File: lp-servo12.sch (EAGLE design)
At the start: 63 parts, among them J1 M10", J2 M10", J3 M10", J4 M10", U1 TPS54526PWP, U2 LMV358

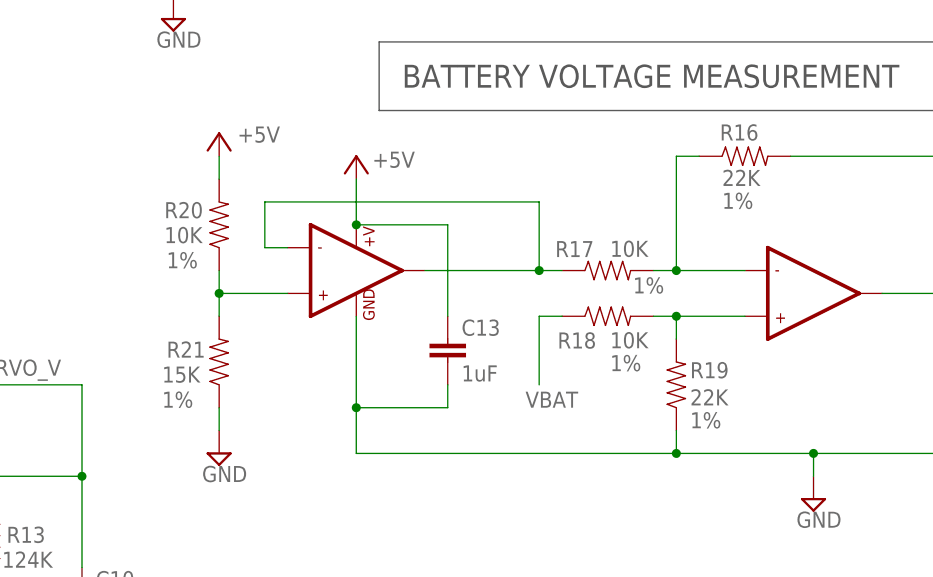
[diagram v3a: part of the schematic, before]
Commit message: Fixed some resistor values on the voltage measuring op-amp circuit. The orginal values were not correct for a 2S battery (they were for a 1S battery). Updated the bom files to reflect the changes in the resistor values. Net effect is that two 22K resistors go away and 2 30K are added, some ref designators change.
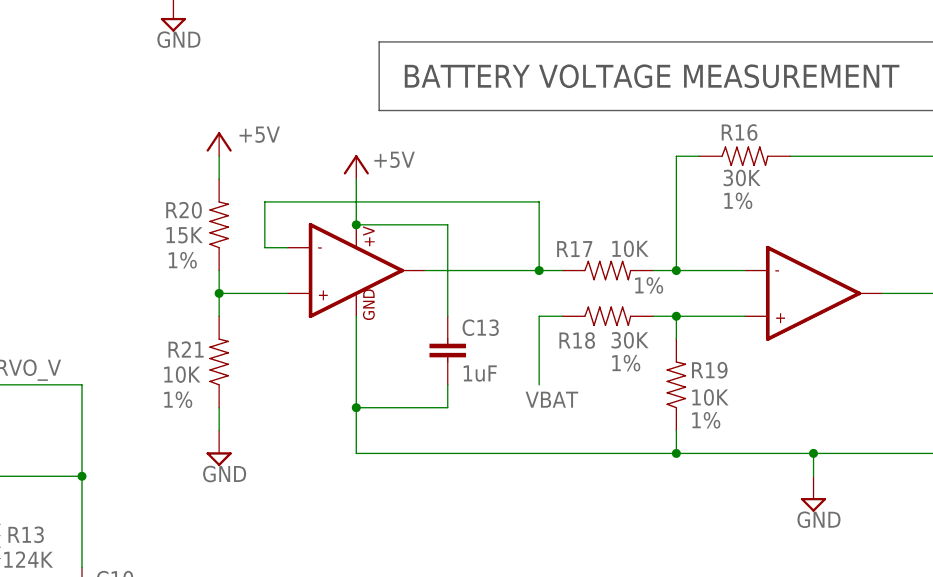
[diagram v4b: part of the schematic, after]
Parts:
- R16: value 22K -> 30K; PARTNO RES_22K_20V_1PCT_0805 -> RES_30K_20V_1PCT_0805
- R18: value 10K -> 30K; PARTNO RES_10K_20V_1PCT_0805 -> RES_30K_20V_1PCT_0805
- R19: value 22K -> 10K; PARTNO RES_22K_20V_1PCT_0805 -> RES_10K_20V_1PCT_0805
- R20: value 10K -> 15K; PARTNO RES_10K_20V_1PCT_0805 -> RES_15K_20V_1PCT_0805
- R21: value 15K -> 10K; PARTNO RES_15K_20V_1PCT_0805 -> RES_10K_20V_1PCT_0805
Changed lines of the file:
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@@
 <attribute name="PARTNO" value="LMV358QDR"/>
 </part>
-<part name="R16" library="SparkFun-Resistors" deviceset="RESISTOR" device="0805-RES" value="22K">
-<attribute name="PARTNO" value="RES_22K_20V_1PCT_0805"/>
+<part name="R16" library="SparkFun-Resistors" deviceset="RESISTOR" device="0805-RES" value="30K">
+<attribute name="PARTNO" value="RES_30K_20V_1PCT_0805"/>
 <attribute name="SIZE" value="(0805)"/>
 <attribute name="TOL" value="1%"/>
@@
 <attribute name="VOLT" value="20V"/>
 </part>
-<part name="R18" library="SparkFun-Resistors" deviceset="RESISTOR" device="0805-RES" value="10K">
+<part name="R18" library="SparkFun-Resistors" deviceset="RESISTOR" device="0805-RES" value="30K">
+<attribute name="PARTNO" value="RES_30K_20V_1PCT_0805"/>
+<attribute name="SIZE" value="(0805)"/>
+<attribute name="TOL" value="1%"/>
+<attribute name="VOLT" value="20V"/>
+</part>
+<part name="R19" library="SparkFun-Resistors" deviceset="RESISTOR" device="0805-RES" value="10K">
 <attribute name="PARTNO" value="RES_10K_20V_1PCT_0805"/>
 <attribute name="SIZE" value="(0805)"/>
@@
 <attribute name="VOLT" value="20V"/>
 </part>
-<part name="R19" library="SparkFun-Resistors" deviceset="RESISTOR" device="0805-RES" value="22K">
-<attribute name="PARTNO" value="RES_22K_20V_1PCT_0805"/>
+<part name="SUPPLY13" library="supply2" deviceset="GND" device=""/>
+<part name="R20" library="SparkFun-Resistors" deviceset="RESISTOR" device="0805-RES" value="15K">
+<attribute name="PARTNO" value="RES_15K_20V_1PCT_0805"/>
 <attribute name="SIZE" value="(0805)"/>
 <attribute name="TOL" value="1%"/>
 <attribute name="VOLT" value="20V"/>
 </part>
-<part name="SUPPLY13" library="supply2" deviceset="GND" device=""/>
-<part name="R20" library="SparkFun-Resistors" deviceset="RESISTOR" device="0805-RES" value="10K">
+<part name="R21" library="SparkFun-Resistors" deviceset="RESISTOR" device="0805-RES" value="10K">
 <attribute name="PARTNO" value="RES_10K_20V_1PCT_0805"/>
 <attribute name="SIZE" value="(0805)"/>
 <attribute name="TOL" value="1%"/>
-<attribute name="VOLT" value="20V"/>
-</part>
-<part name="R21" library="SparkFun-Resistors" deviceset="RESISTOR" device="0805-RES" value="15K">
-<attribute name="PARTNO" value="RES_15K_20V_1PCT_0805"/>
-<attribute name="SIZE" value="(0805)"/>
-<attribute name="TOL" value="1%"/>

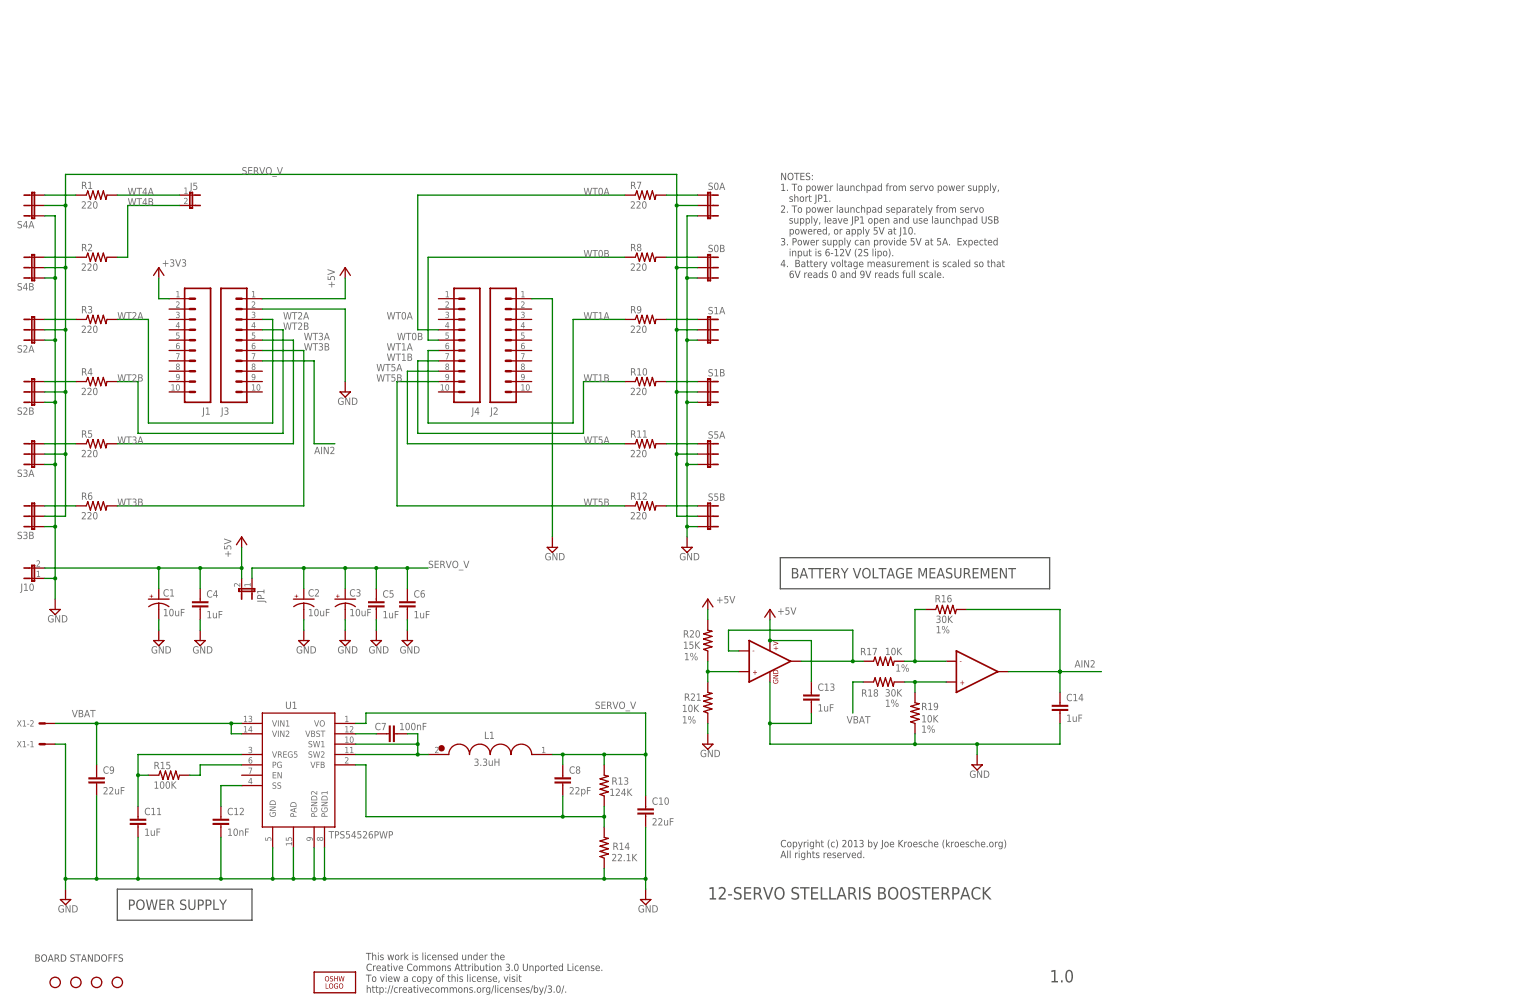
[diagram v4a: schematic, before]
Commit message: Fixed missing pullup on enable line and unconnectd trace on feeback signal for power supply.  Those were the two known bugs. Also moved one of the moounting holes and moved the power connector around so that it would not overhang the edge of the board, and also changed the orientation to come out the top instead of the side.
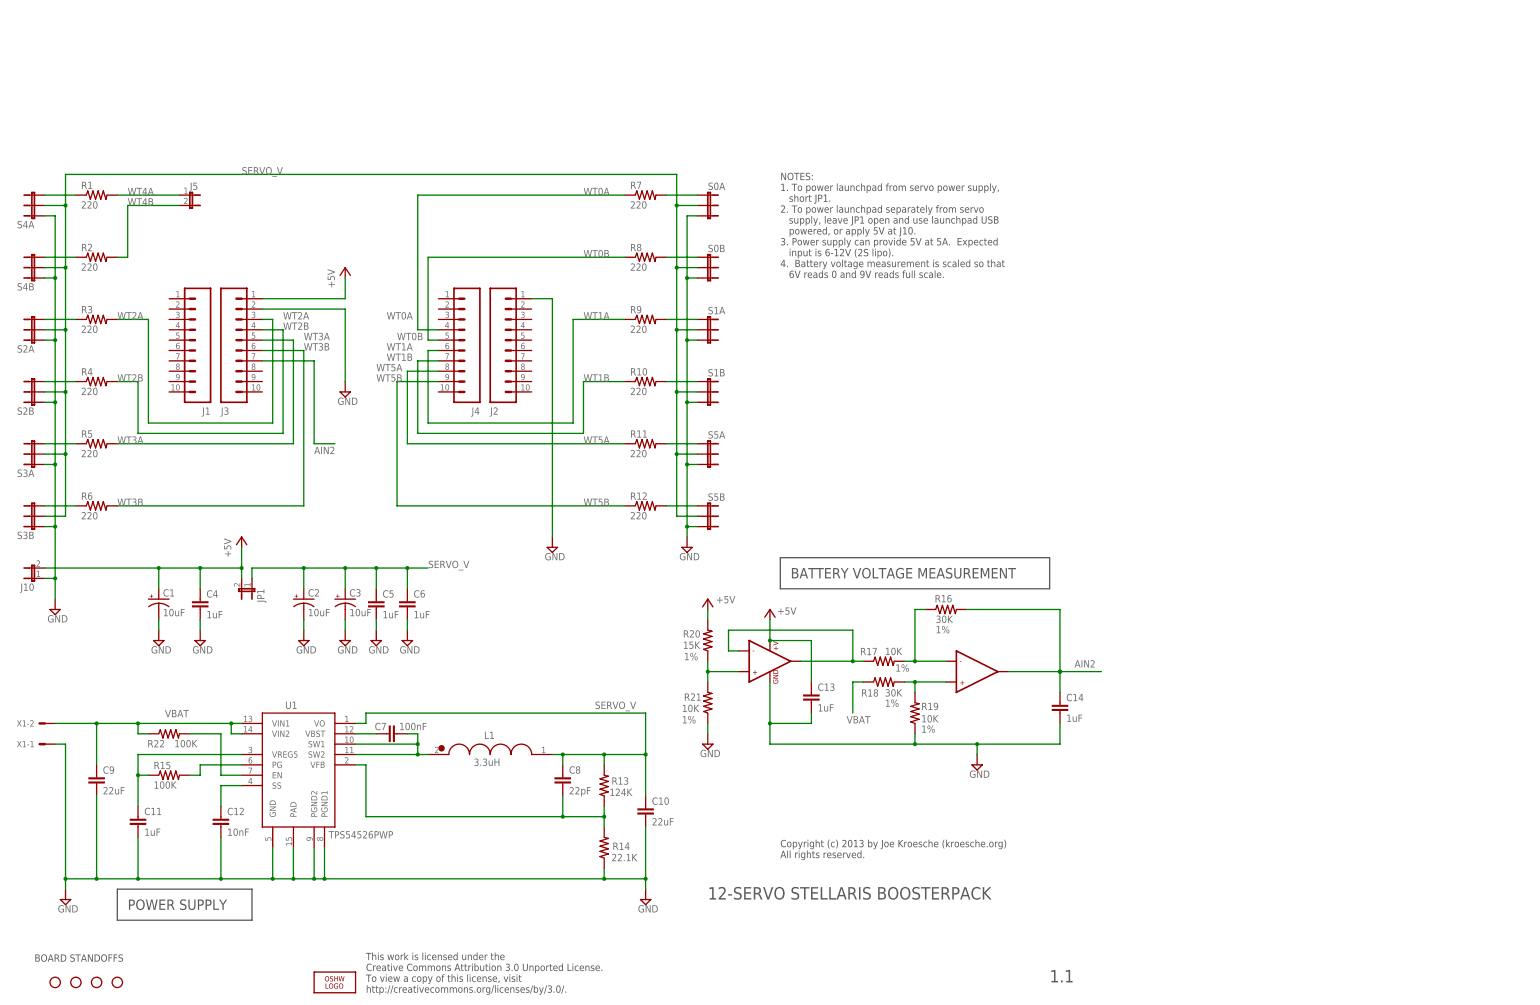
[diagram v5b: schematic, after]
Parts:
- added R22: 100K, SparkFun-Resistors:RESISTOR0805-RES
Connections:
- removed net +3V3: J1.1
- new net N$19: R22.2, U1.EN
- net VBAT: now also R22.1
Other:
- note added: "1.1"
- note removed: "1.0"
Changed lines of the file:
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@@
 <part name="SUPPLY1" library="supply2" deviceset="GND" device=""/>
 <part name="SUPPLY2" library="supply2" deviceset="GND" device=""/>
-<part name="+3V1" library="supply1" deviceset="+3V3" device=""/>
 <part name="P+1" library="supply1" deviceset="+5V" device=""/>
 <part name="SUPPLY3" library="supply2" deviceset="GND" device=""/>
@@
 </part>
 <part name="FRAME2" library="frames" deviceset="FRAME_A_L" device=""/>
+<part name="R22" library="SparkFun-Resistors" deviceset="RESISTOR" device="0805-RES" value="100K">
+<attribute name="PARTNO" value="RES_100K_20V_1PCT_0805"/>
+<attribute name="RATE" value="1/8W"/>
+<attribute name="SIZE" value="(0805)"/>
+<attribute name="TOL" value="1%"/>
+<attribute name="VOLT" value="20V"/>
+</part>
 </parts>
 <sheets>
@@
 4.  Battery voltage measurement is scaled so that
    6V reads 0 and 9V reads full scale.</text>
-<text x="261.62" y="7.62" size="3.048" layer="97" font="vector">1.0</text>
+<text x="261.62" y="7.62" size="3.048" layer="97" font="vector">1.1</text>
 </plain>
 <instances>
 <instance part="SUPPLY1" gate="GND" x="88.9" y="152.4"/>
 <instance part="SUPPLY2" gate="GND" x="139.7" y="114.3"/>
-<instance part="+3V1" gate="G$1" x="43.18" y="182.88" smashed="yes">
-<attribute name="VALUE" x="43.942" y="183.134" size="1.778" layer="96"/>
-</instance>
 <instance part="P+1" gate="1" x="88.9" y="182.88"/>
 <instance part="SUPPLY3" gate="GND" x="17.78" y="99.06"/>
@@
 <instance part="FRAME2" gate="G$1" x="0" y="0"/>
 <instance part="FRAME2" gate="G$2" x="172.72" y="0"/>
+<instance part="R22" gate="G$1" x="45.72" y="68.58" smashed="yes">
+<attribute name="PARTNO" x="45.72" y="68.58" size="1.778" layer="96" display="off"/>
+<attribute name="RATE" x="45.72" y="68.58" size="1.778" layer="96" display="off"/>
+<attribute name="SIZE" x="45.72" y="68.58" size="1.778" layer="96" display="off"/>
+<attribute name="TOL" x="45.72" y="68.58" size="1.778" layer="96" display="off"/>
+<attribute name="VOLT" x="45.72" y="68.58" size="1.778" layer="96" display="off"/>
+<attribute name="NAME" x="40.386" y="65.2526" size="1.778" layer="95"/>
+<attribute name="VALUE" x="46.99" y="65.278" size="1.778" layer="96"/>
+</instance>
 </instances>
 <busses>
@@
 <pinref part="SUPPLY14" gate="GND" pin="GND"/>
 <wire x1="177.8" y1="71.12" x2="177.8" y2="68.58" width="0.1524" layer="91"/>
-</segment>
-</net>
-<net name="+3V3" class="0">
-<segment>
-<pinref part="+3V1" gate="G$1" pin="+3V3"/>
-<wire x1="43.18" y1="175.26" x2="43.18" y2="180.34" width="0.1524" layer="91"/>
-<pinref part="J1" gate="G$1" pin="1"/>
-<wire x1="43.18" y1="175.26" x2="45.72" y2="175.26" width="0.1524" layer="91"/>
 </segment>
 </net>
@@
 <pinref part="C9" gate="G$1" pin="1"/>
 <wire x1="63.5" y1="71.12" x2="60.96" y2="71.12" width="0.1524" layer="91"/>
-<wire x1="60.96" y1="71.12" x2="27.94" y2="71.12" width="0.1524" layer="91"/>
+<wire x1="60.96" y1="71.12" x2="38.1" y2="71.12" width="0.1524" layer="91"/>
+<wire x1="38.1" y1="71.12" x2="27.94" y2="71.12" width="0.1524" layer="91"/>
 <wire x1="27.94" y1="71.12" x2="27.94" y2="60.96" width="0.1524" layer="91"/>
 <pinref part="U1" gate="G$1" pin="VIN2"/>
@@
 <wire x1="60.96" y1="68.58" x2="60.96" y2="71.12" width="0.1524" layer="91"/>
 <junction x="60.96" y="71.12"/>
-<label x="21.844" y="72.644" size="1.778" layer="95"/>
+<label x="44.704" y="72.644" size="1.778" layer="95"/>
+<pinref part="R22" gate="G$1" pin="1"/>
+<wire x1="40.64" y1="68.58" x2="38.1" y2="68.58" width="0.1524" layer="91"/>
+<wire x1="38.1" y1="68.58" x2="38.1" y2="71.12" width="0.1524" layer="91"/>
+<junction x="38.1" y="71.12"/>
 <pinref part="X1" gate="-2" pin="S"/>
-<wire x1="17.78" y1="71.12" x2="27.94" y2="71.12" width="0.1524" layer="91"/>
+<wire x1="27.94" y1="71.12" x2="17.78" y2="71.12" width="0.1524" layer="91"/>
 <junction x="27.94" y="71.12"/>
 </segment>
@@
 </segment>
 </net>
+<net name="N$19" class="0">
+<segment>
+<pinref part="U1" gate="G$1" pin="EN"/>
+<wire x1="63.5" y1="58.42" x2="58.42" y2="58.42" width="0.1524" layer="91"/>
+<wire x1="58.42" y1="58.42" x2="58.42" y2="68.58" width="0.1524" layer="91"/>
+<pinref part="R22" gate="G$1" pin="2"/>
+<wire x1="50.8" y1="68.58" x2="58.42" y2="68.58" width="0.1524" layer="91"/>
+</segment>
+</net>
 </nets>
 </sheet>
 </sheets>
+<errors>
+</errors>
 </schematic>
 </drawing>
